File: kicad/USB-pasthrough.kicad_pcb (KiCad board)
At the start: 4 copper layers, 40 x 80 mm, 93 parts, among them J1 USB_Power, J2 USB_C, J3 Cortex Debug, J4 Power_Sel, J5 SPI Display, J6 SWD, J7 USB_A, J8 MicroSD, SW1 Boot0, SW2 Reset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

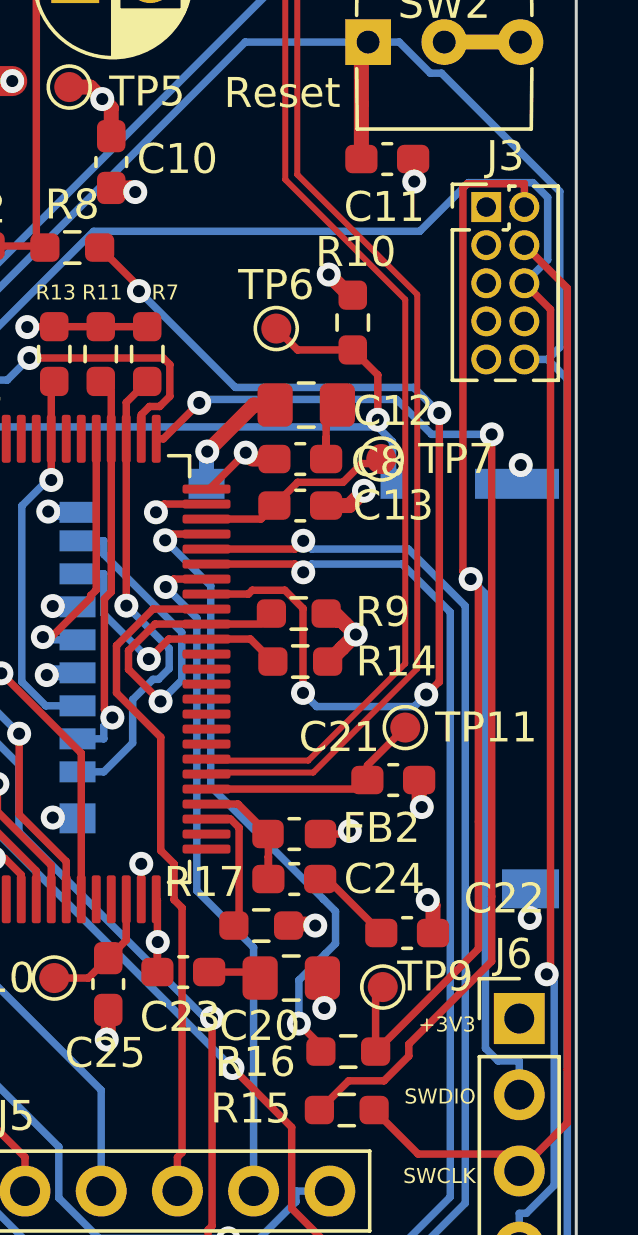
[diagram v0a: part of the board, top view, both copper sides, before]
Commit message: Reroute SWDIO trace that was awkward
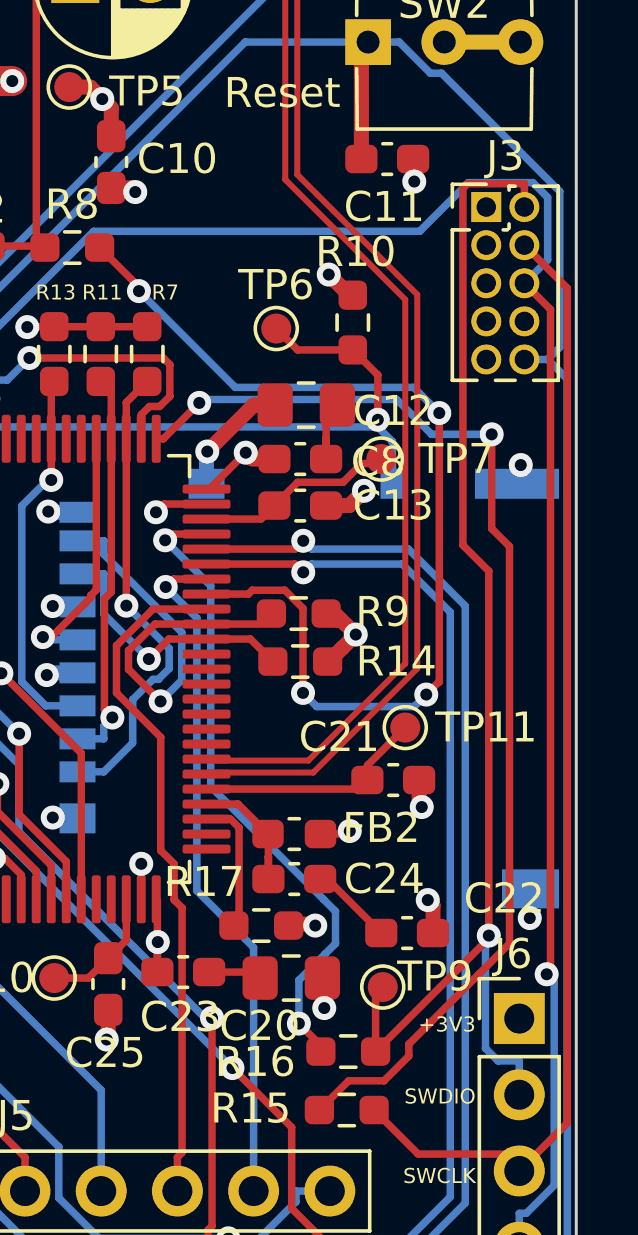
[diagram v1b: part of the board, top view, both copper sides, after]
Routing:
- net /SWDIO: track 53.8 -> 42.1 mm
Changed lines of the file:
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@@
   (segment (start 120.355 105.886) (end 112.794 98.3246) (width 0.25) (layer "B.Cu") (net 24))
   (segment (start 133.3125 100.8375) (end 133.55 100.6) (width 0.25) (layer "F.Cu") (net 25))
-  (segment (start 136.738 87.2574) (end 136.738 95.0883) (width 0.25) (layer "F.Cu") (net 25))
-  (segment (start 138.27 73.8231) (end 136.359 73.8231) (width 0.25) (layer "F.Cu") (net 25))
-  (segment (start 138.27 74.6) (end 138.27 73.8231) (width 0.25) (layer "F.Cu") (net 25))
+  (segment (start 137.084906 86.734906) (end 136.222 85.872) (width 0.25) (layer "F.Cu") (net 25))
+  (segment (start 138.27 73.8231) (end 138.27 74.6) (width 0.25) (layer "F.Cu") (net 25))
+  (segment (start 136.359 73.8231) (end 138.27 73.8231) (width 0.25) (layer "F.Cu") (net 25))
+  (segment (start 136.222 73.9598) (end 136.359 73.8231) (width 0.25) (layer "F.Cu") (net 25))
   (segment (start 133.3125 102.75) (end 133.3125 100.8375) (width 0.25) (layer "F.Cu") (net 25))
-  (segment (start 136.222 86.7414) (end 136.4806 87) (width 0.25) (layer "F.Cu") (net 25))
-  (segment (start 136.738 95.0883) (end 136.738 99.3245) (width 0.25) (layer "F.Cu") (net 25))
-  (segment (start 136.359 73.8231) (end 136.222 73.9598) (width 0.25) (layer "F.Cu") (net 25))
-  (segment (start 136.222 73.9598) (end 136.222 86.7414) (width 0.25) (layer "F.Cu") (net 25))
-  (segment (start 136.738 99.3245) (end 133.3125 102.75) (width 0.25) (layer "F.Cu") (net 25))
-  (segment (start 136.4806 87) (end 136.738 87.2574) (width 0.25) (layer "F.Cu") (net 25))
-  (via (at 136.4806 87) (size 0.8) (drill 0.4) (layers "F.Cu" "B.Cu") (net 25))
-  (segment (start 136.9731 87.4925) (end 136.4806 87) (width 0.25) (layer "B.Cu") (net 25))
+  (segment (start 136.222 85.872) (end 136.222 73.9598) (width 0.25) (layer "F.Cu") (net 25))
+  (segment (start 133.3125 102.75) (end 137.084906 98.977594) (width 0.25) (layer "F.Cu") (net 25))
+  (segment (start 137.084906 98.884906) (end 137.084906 86.734906) (width 0.25) (layer "F.Cu") (net 25))
+  (segment (start 137.084906 98.977594) (end 137.084906 98.884906) (width 0.25) (layer "F.Cu") (net 25))
+  (via (at 137.084906 98.884906) (size 0.8) (drill 0.4) (layers "F.Cu" "B.Cu") (net 25))
+  (segment (start 136.9731 98.996712) (end 137.084906 98.884906) (width 0.25) (layer "B.Cu") (net 25))
+  (segment (start 136.9731 102.6406) (end 136.9731 98.996712) (width 0.25) (layer "B.Cu") (net 25))
   (segment (start 137.3956 103.0631) (end 136.9731 102.6406) (width 0.25) (layer "B.Cu") (net 25))
   (segment (start 138.1 104.19) (end 138.1 103.0631) (width 0.25) (layer "B.Cu") (net 25))
   (segment (start 138.1 103.0631) (end 137.3956 103.0631) (width 0.25) (layer "B.Cu") (net 25))
-  (segment (start 136.9731 102.6406) (end 136.9731 87.4925) (width 0.25) (layer "B.Cu") (net 25))
   (segment (start 138.1 106.73) (end 138.1 106.1665) (width 0.25) (layer "F.Cu") (net 26))
   (segment (start 139.701 77.3011) (end 138.27 75.87) (width 0.25) (layer "F.Cu") (net 26))
@@
   (segment (start 127.816 87.227) (end 126.296 85.7071) (width 0.25) (layer "B.Cu") (net 46))
   (segment (start 131.975 99.1502) (end 131.975 98.075) (width 0.25) (layer "B.Cu") (net 46))
+  (segment (start 137.775 99.1487) (end 137.775 85.913) (width 0.25) (layer "F.Cu") (net 47))
+  (segment (start 136.76185 100.16185) (end 134.4179 102.5058) (width 0.25) (layer "F.Cu") (net 47))
   (segment (start 132.4125 103.725) (end 131.4375 104.7) (width 0.25) (layer "F.Cu") (net 47))
   (segment (start 134.4179 102.5058) (end 134.4179 102.8995) (width 0.25) (layer "F.Cu") (net 47))
   (segment (start 133.5924 103.725) (end 132.4125 103.725) (width 0.25) (layer "F.Cu") (net 47))
   (segment (start 127.434 81.1286) (end 126.238 82.325) (width 0.25) (layer "F.Cu") (net 47))
-  (segment (start 137.181 97.5838) (end 137.181 99.7427) (width 0.25) (layer "F.Cu") (net 47))
+  (segment (start 136.76185 100.16185) (end 137.775 99.1487) (width 0.25) (layer "F.Cu") (net 47))
+  (segment (start 137.775 85.913) (end 137.181 85.319) (width 0.25) (layer "F.Cu") (net 47))
   (segment (start 134.4179 102.8995) (end 133.5924 103.725) (width 0.25) (layer "F.Cu") (net 47))
-  (segment (start 137.181 99.7427) (end 134.4179 102.5058) (width 0.25) (layer "F.Cu") (net 47))
   (segment (start 126.238 82.325) (end 126 82.325) (width 0.25) (layer "F.Cu") (net 47))
-  (segment (start 137.181 97.5838) (end 137.181 82.1764) (width 0.25) (layer "F.Cu") (net 47))
+  (segment (start 137.181 85.319) (end 137.181 82.1764) (width 0.25) (layer "F.Cu") (net 47))
   (via (at 137.181 82.1764) (size 0.8) (drill 0.4) (layers "F.Cu" "B.Cu") (net 47))
   (via (at 127.434 81.1286) (size 0.8) (drill 0.4) (layers "F.Cu" "B.Cu") (net 47))

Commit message: Clean up traces
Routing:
- net /PA13: track 21.5 -> 20.5 mm
- net /LED5_B: track 58.8 -> 58.0 mm
- net /LED5_R: track 64.1 -> 63.4 mm

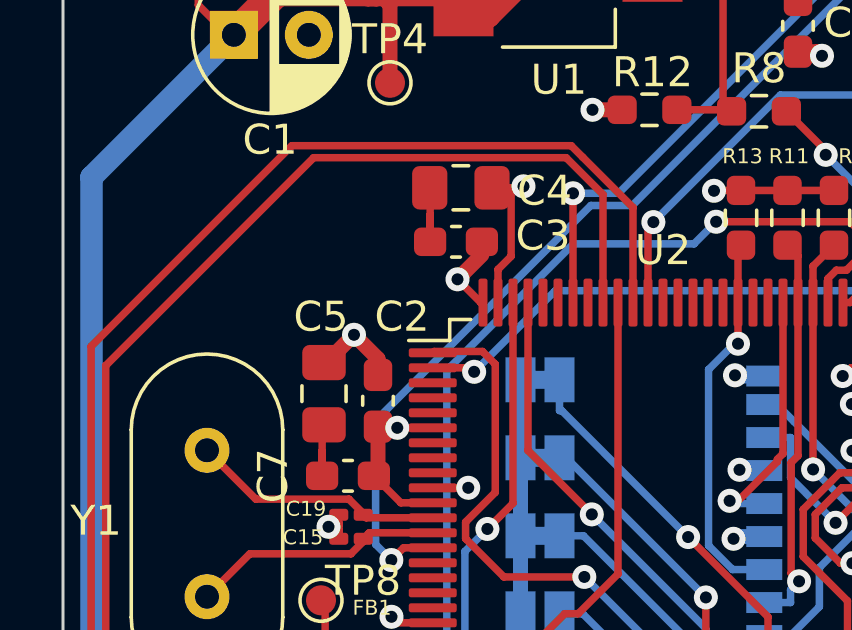
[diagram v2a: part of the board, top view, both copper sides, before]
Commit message: Add U1 pi 1 mark
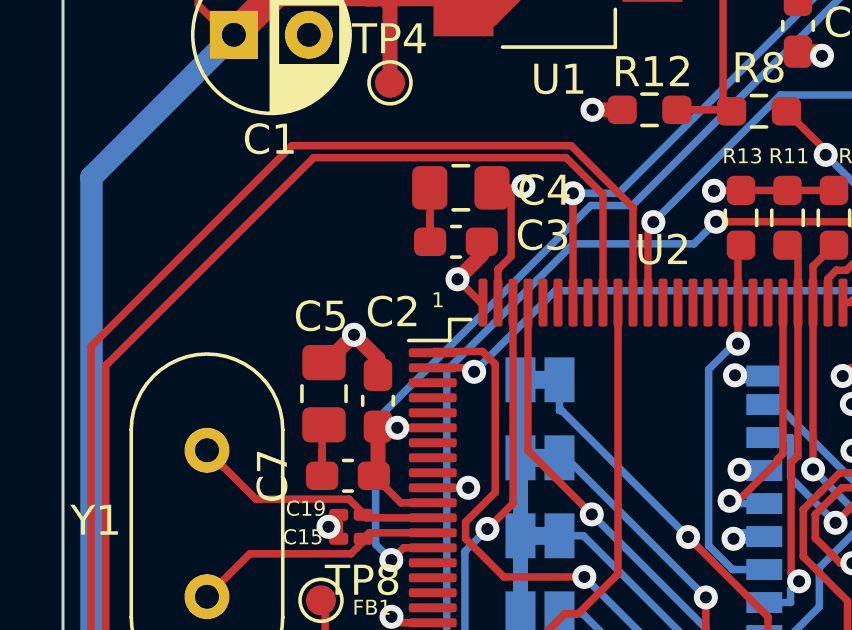
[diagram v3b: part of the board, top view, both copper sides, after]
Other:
- board text added: "1"
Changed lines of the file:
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@@
     (property "Sheetname" "")
     (attr smd)
-    (fp_text reference "C2" (at -2.8 -0.8 180) (layer "F.SilkS")
+    (fp_text reference "C2" (at -2.95 -0.5 180) (layer "F.SilkS")
       (effects (font (size 1 1) (thickness 0.15)))
     )
@@
     (effects (font (size 0.5 0.5) (thickness 0.1)) (justify right))
   )
+  (gr_text "1" (at 112.5 82.25) (layer "F.SilkS")
+    (effects (font (size 0.5 0.5) (thickness 0.1)))
+  )
   (gr_text "+3V3" (at 136.65 101.85) (layer "F.SilkS")

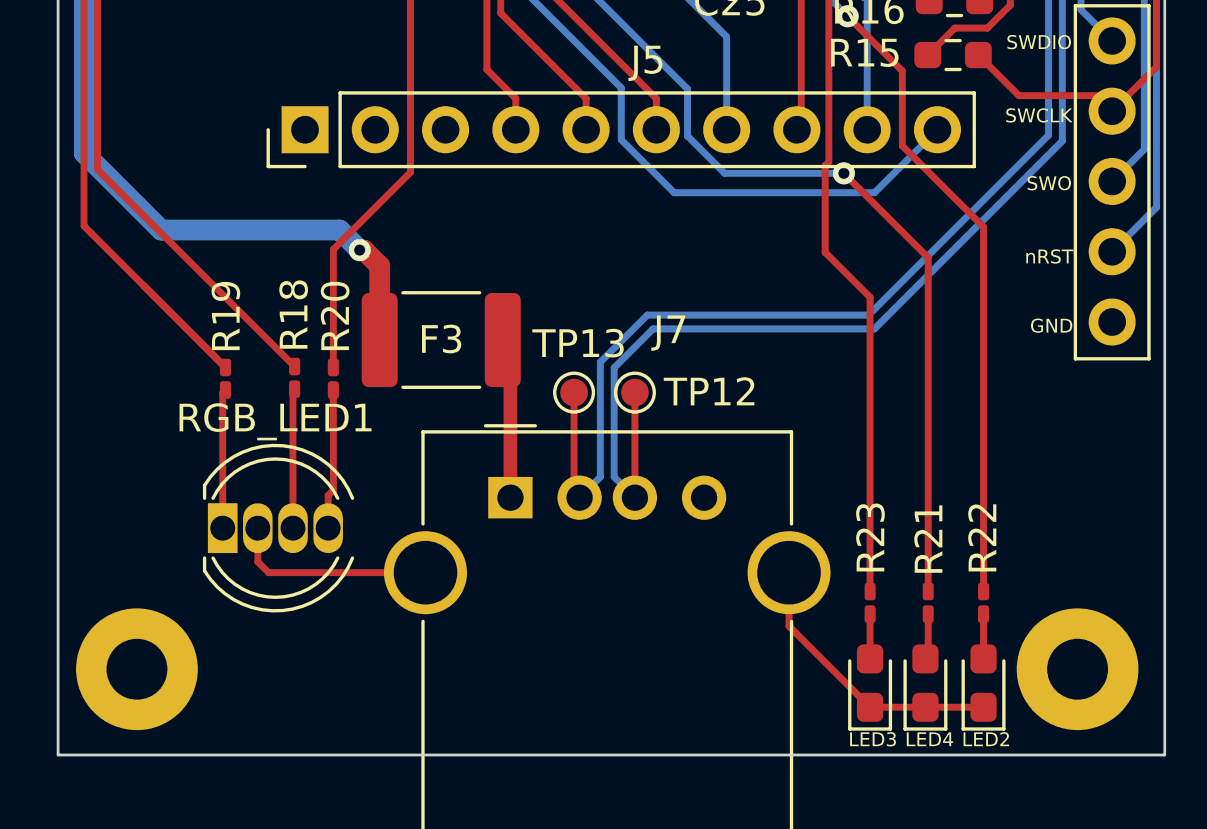
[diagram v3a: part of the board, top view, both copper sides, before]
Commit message: Change incorrect metric footprints to imperial
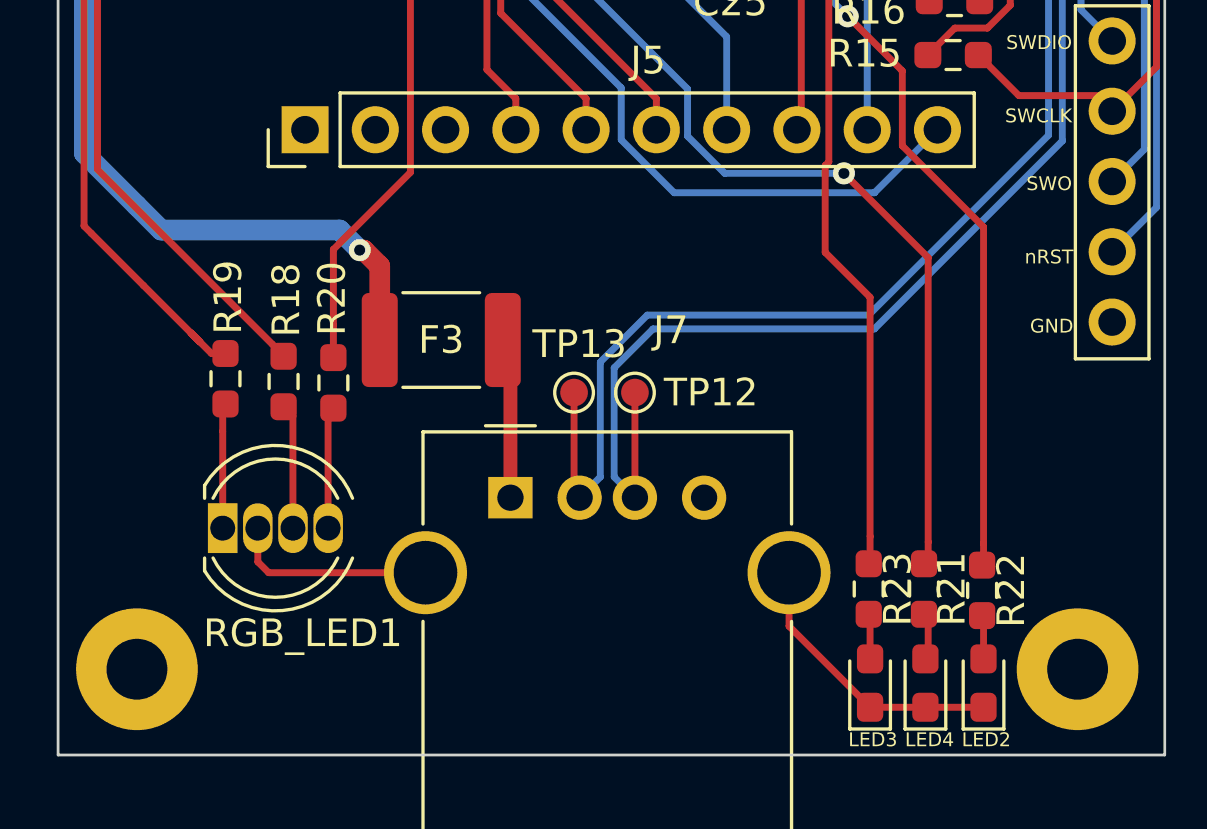
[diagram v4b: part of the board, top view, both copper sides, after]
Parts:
- R18, R19, R20, R21, R22, R23: footprint Resistor_SMD:R_0201_0603Metric_Pad0.64x0.40mm_HandSolder -> Resistor_SMD:R_0603_1608Metric_Pad0.98x0.95mm_HandSolder
- moved R21 0.52 mm to (131.3, 124.0)
- moved R23 0.50 mm to (129.3, 124.0)
- moved R22 0.45 mm to (133.4, 124.0)
- moved R18 0.42 mm to (108.2, 116.5)
- moved R20 0.15 mm to (110.0, 116.5)
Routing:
- net /LED5_R: track 63.4 -> 59.9 mm
- net /LED2: track 47.8 -> 46.8 mm
- net /LED4: track 52.3 -> 51.5 mm
- net /LED3: track 52.4 -> 51.6 mm
- net /LED5_B: track 58.0 -> 57.3 mm
- net Net-(R20-Pad1): track 5.07 -> 4.42 mm
- net Net-(R18-Pad1): track 5.05 -> 4.53 mm
- net /LED5_G: track 37.6 -> 37.1 mm
- net Net-(R19-Pad2): track 5.03 -> 4.53 mm
